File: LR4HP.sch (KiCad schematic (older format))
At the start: 15 parts

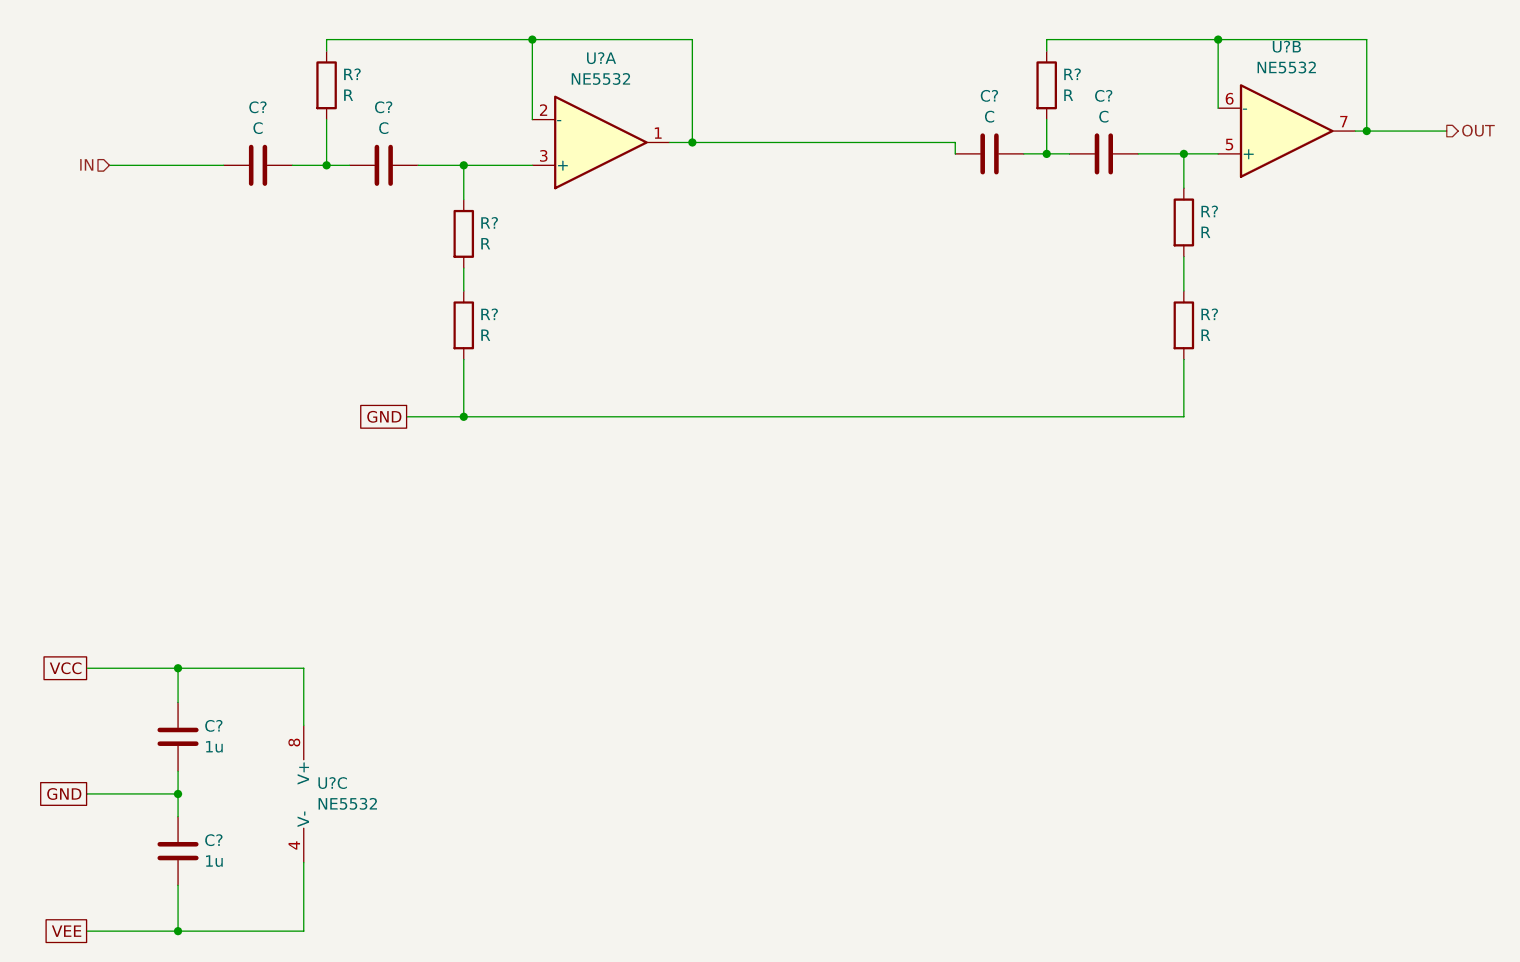
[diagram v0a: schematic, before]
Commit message: improved PSU, gain up front, reordered filter stages, shrunk rumble filter
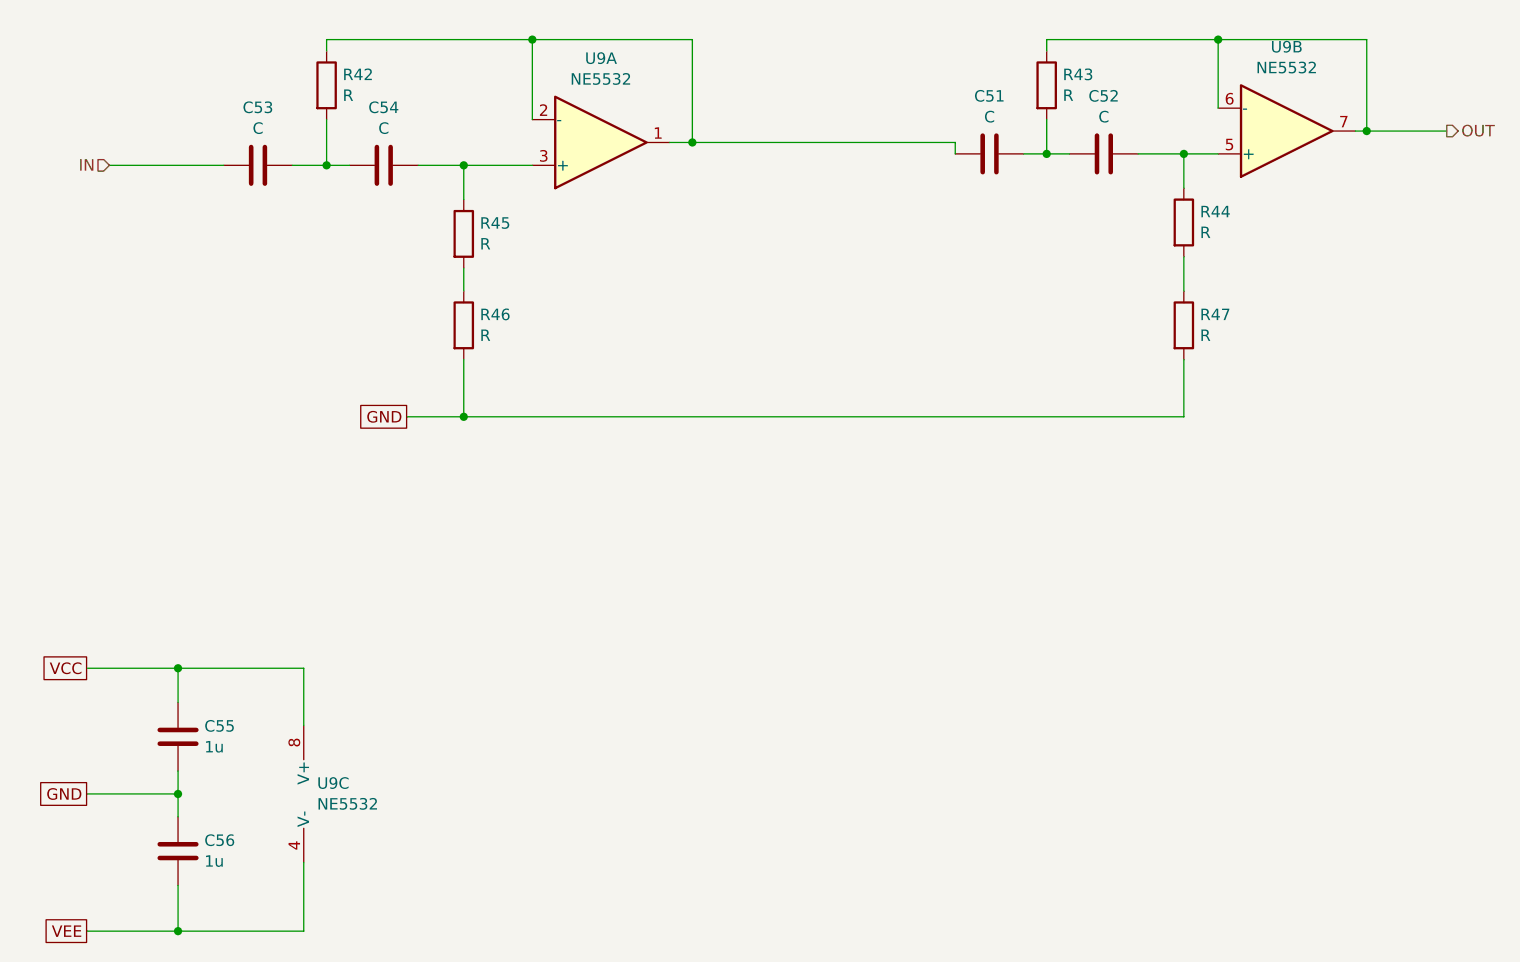
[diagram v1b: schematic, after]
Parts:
- gave numbers to parts that had none: 13

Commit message: added buffered volume pot, and fixed subsonic filter added signal taps for external transforms/filters to be added later
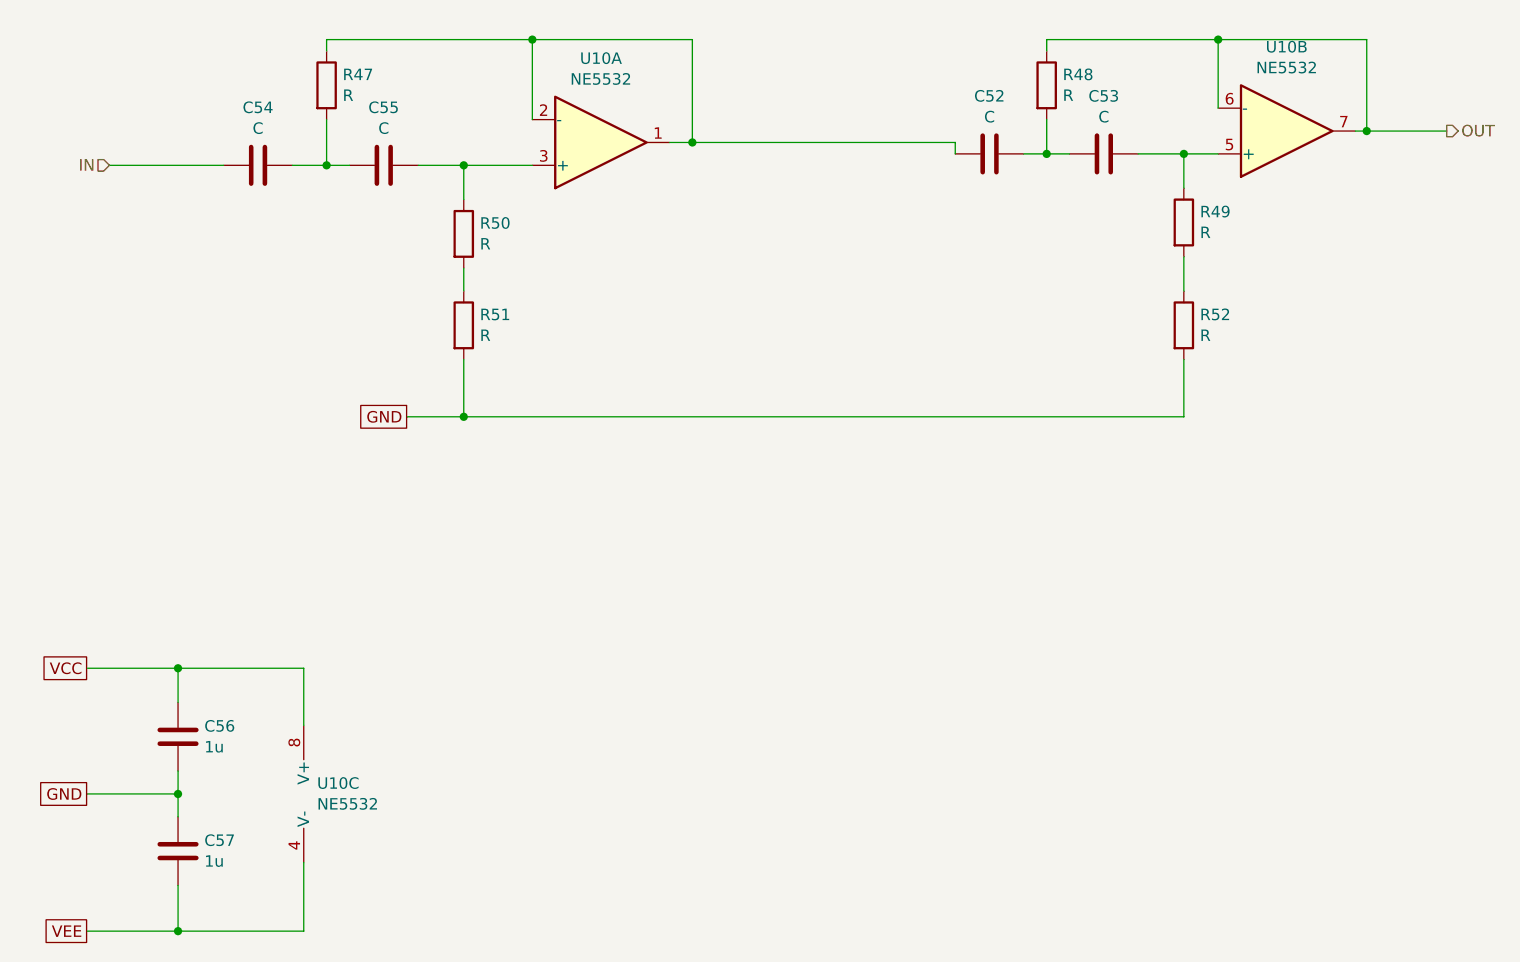
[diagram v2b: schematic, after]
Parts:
- renumbered C45 to C46, C46 to C47, C47 to C48, C48 to C49, C49 to C50, C50 to C51, R36 to R41, R37 to R42, R38 to R43, R39 to R44, R40 to R45, R41 to R46, U8 to U9

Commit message: inverted LF processing chain, now with BW2 subsonic filter
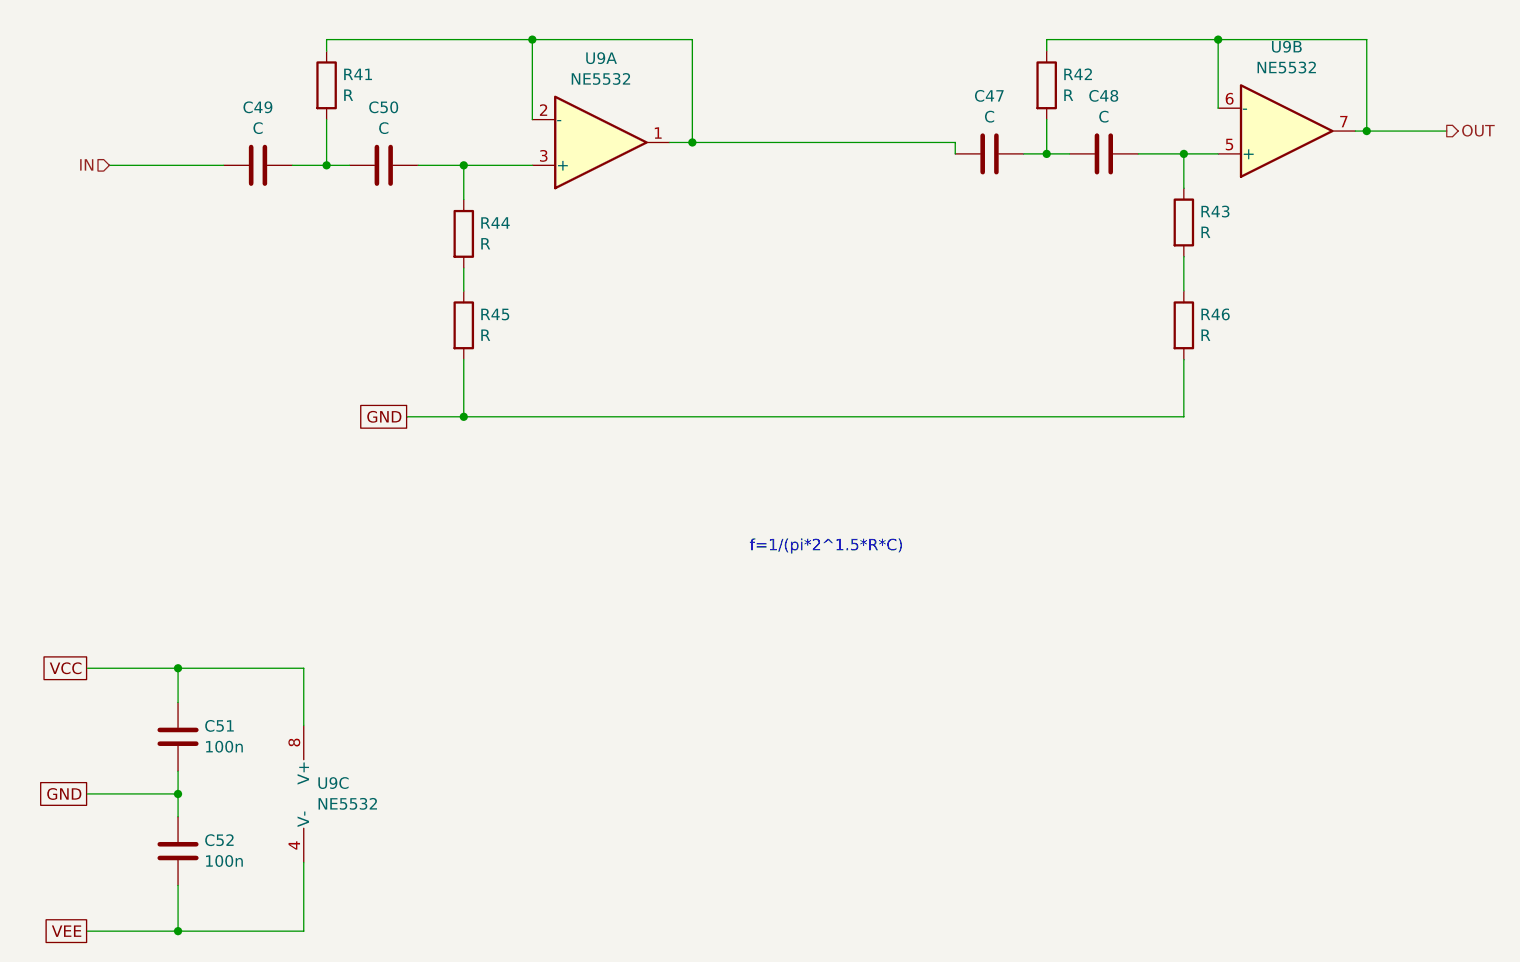
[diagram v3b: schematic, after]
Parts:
- C51: renamed from C50; value 1u -> 100n
- C52: renamed from C51; value 1u -> 100n
- renumbered C46 to C47, C47 to C48, C48 to C49, C49 to C50
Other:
- note added: "f=1/(pi*2^1.5*R*C)"
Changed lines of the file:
@@
 $Descr A4 11693 8268
 encoding utf-8
-Sheet 9 19
+Sheet 8 17
 Title "4th Order Linkwitz-Riley High-Pass"
 Date "2021-10-03"
@@
 AR Path="/61597701/61581F20" Ref="U10"  Part="3"
 AR Path="/615C4B54/61581F20" Ref="U?"  Part="3"
-F 0 "U10" H 3358 4996 50  0000 L CNN
+F 0 "U9" H 3358 4996 50  0000 L CNN
 F 1 "NE5532" H 3358 4905 50  0000 L CNN
 F 2 "Housings_DIP:DIP-8_W7.62mm_Socket" H 3400 4950 50  0001 C CNN
@@
 $EndComp
 $Comp
-L Device:C C51
+L Device:C C52
 U 1 1 615A630E
 P 2750 5200
-AR Path="/6157B871/615A630E" Ref="C51"  Part="1"
-AR Path="/615961F1/615A630E" Ref="C17"  Part="1"
-AR Path="/61596D2A/615A630E" Ref="C31"  Part="1"
-AR Path="/61597701/615A630E" Ref="C57"  Part="1"
+AR Path="/6157B871/615A630E" Ref="C52"  Part="1"
+AR Path="/615961F1/615A630E" Ref="C18"  Part="1"
+AR Path="/61596D2A/615A630E" Ref="C32"  Part="1"
+AR Path="/61597701/615A630E" Ref="C58"  Part="1"
 AR Path="/615C4B54/615A630E" Ref="C?"  Part="1"
-F 0 "C57" H 2865 5246 50  0000 L CNN
-F 1 "1u" H 2865 5155 50  0000 L CNN
+F 0 "C52" H 2865 5246 50  0000 L CNN
+F 1 "100n" H 2865 5155 50  0000 L CNN
 F 2 "Capacitors_SMD:C_0805" H 2788 5050 50  0001 C CNN
 F 3 "~" H 2750 5200 50  0001 C CNN
@@
 AR Path="/61597701/61593BE2" Ref="R51"  Part="1"
 AR Path="/615C4B54/61593BE2" Ref="R?"  Part="1"
-F 0 "R51" H 4070 2946 50  0000 L CNN
+F 0 "R45" H 4070 2946 50  0000 L CNN
 F 1 "R" H 4070 2855 50  0000 L CNN
 F 2 "Resistors_SMD:R_0805" V 3930 2900 50  0001 C CNN
@@
 AR Path="/61597701/615935AE" Ref="R50"  Part="1"
 AR Path="/615C4B54/615935AE" Ref="R?"  Part="1"
-F 0 "R50" H 4070 2546 50  0000 L CNN
+F 0 "R44" H 4070 2546 50  0000 L CNN
 F 1 "R" H 4070 2455 50  0000 L CNN
 F 2 "Resistors_SMD:R_0805" V 3930 2500 50  0001 C CNN
@@
 AR Path="/61597701/61592F52" Ref="R47"  Part="1"
 AR Path="/615C4B54/61592F52" Ref="R?"  Part="1"
-F 0 "R47" H 3470 1896 50  0000 L CNN
+F 0 "R41" H 3470 1896 50  0000 L CNN
 F 1 "R" H 3470 1805 50  0000 L CNN
 F 2 "Resistors_SMD:R_0805" V 3330 1850 50  0001 C CNN
@@
 $EndComp
 $Comp
-L Device:C C49
+L Device:C C50
 U 1 1 61590C79
 P 3650 2200
-AR Path="/6157B871/61590C79" Ref="C49"  Part="1"
-AR Path="/615961F1/61590C79" Ref="C15"  Part="1"
-AR Path="/61596D2A/61590C79" Ref="C29"  Part="1"
-AR Path="/61597701/61590C79" Ref="C55"  Part="1"
+AR Path="/6157B871/61590C79" Ref="C50"  Part="1"
+AR Path="/615961F1/61590C79" Ref="C16"  Part="1"
+AR Path="/61596D2A/61590C79" Ref="C30"  Part="1"
+AR Path="/61597701/61590C79" Ref="C56"  Part="1"
 AR Path="/615C4B54/61590C79" Ref="C?"  Part="1"
-F 0 "C55" V 3398 2200 50  0000 C CNN
+F 0 "C50" V 3398 2200 50  0000 C CNN
 F 1 "C" V 3489 2200 50  0000 C CNN
 F 2 "Capacitors_SMD:C_1210_HandSoldering" H 3688 2050 50  0001 C CNN
@@
 $EndComp
 $Comp
-L Device:C C48
+L Device:C C49
 U 1 1 6158BBA5
 P 3100 2200
-AR Path="/6157B871/6158BBA5" Ref="C48"  Part="1"
-AR Path="/615961F1/6158BBA5" Ref="C14"  Part="1"
-AR Path="/61596D2A/6158BBA5" Ref="C28"  Part="1"
-AR Path="/61597701/6158BBA5" Ref="C54"  Part="1"
+AR Path="/6157B871/6158BBA5" Ref="C49"  Part="1"
+AR Path="/615961F1/6158BBA5" Ref="C15"  Part="1"
+AR Path="/61596D2A/6158BBA5" Ref="C29"  Part="1"
+AR Path="/61597701/6158BBA5" Ref="C55"  Part="1"
 AR Path="/615C4B54/6158BBA5" Ref="C?"  Part="1"
-F 0 "C54" V 2848 2200 50  0000 C CNN
+F 0 "C49" V 2848 2200 50  0000 C CNN
 F 1 "C" V 2939 2200 50  0000 C CNN
 F 2 "Capacitors_SMD:C_1210_HandSoldering" H 3138 2050 50  0001 C CNN
@@
 AR Path="/61597701/61581F14" Ref="U10"  Part="1"
 AR Path="/615C4B54/61581F14" Ref="U?"  Part="1"
-F 0 "U10" H 4600 1733 50  0000 C CNN
+F 0 "U9" H 4600 1733 50  0000 C CNN
 F 1 "NE5532" H 4600 1824 50  0000 C CNN
 F 2 "Housings_DIP:DIP-8_W7.62mm_Socket" H 4600 2100 50  0001 C CNN
@@
 $EndComp
 $Comp
-L Device:C C47
+L Device:C C48
 U 1 1 615B29CF
 P 6800 2150
-AR Path="/6157B871/615B29CF" Ref="C47"  Part="1"
-AR Path="/615961F1/615B29CF" Ref="C13"  Part="1"
-AR Path="/61596D2A/615B29CF" Ref="C27"  Part="1"
-AR Path="/61597701/615B29CF" Ref="C53"  Part="1"
+AR Path="/6157B871/615B29CF" Ref="C48"  Part="1"
+AR Path="/615961F1/615B29CF" Ref="C14"  Part="1"
+AR Path="/61596D2A/615B29CF" Ref="C28"  Part="1"
+AR Path="/61597701/615B29CF" Ref="C54"  Part="1"
 AR Path="/615C4B54/615B29CF" Ref="C?"  Part="1"
-F 0 "C53" V 6548 2150 50  0000 C CNN
+F 0 "C48" V 6548 2150 50  0000 C CNN
 F 1 "C" V 6639 2150 50  0000 C CNN
 F 2 "Capacitors_SMD:C_1210_HandSoldering" H 6838 2000 50  0001 C CNN
@@
 $EndComp
 $Comp
-L Device:C C46
+L Device:C C47
 U 1 1 615B9BE0
 P 6300 2150
-AR Path="/6157B871/615B9BE0" Ref="C46"  Part="1"
-AR Path="/615961F1/615B9BE0" Ref="C12"  Part="1"
-AR Path="/61596D2A/615B9BE0" Ref="C26"  Part="1"
-AR Path="/61597701/615B9BE0" Ref="C52"  Part="1"
+AR Path="/6157B871/615B9BE0" Ref="C47"  Part="1"
+AR Path="/615961F1/615B9BE0" Ref="C13"  Part="1"
+AR Path="/61596D2A/615B9BE0" Ref="C27"  Part="1"
+AR Path="/61597701/615B9BE0" Ref="C53"  Part="1"
 AR Path="/615C4B54/615B9BE0" Ref="C?"  Part="1"
-F 0 "C52" V 6048 2150 50  0000 C CNN
+F 0 "C47" V 6048 2150 50  0000 C CNN
 F 1 "C" V 6139 2150 50  0000 C CNN
 F 2 "Capacitors_SMD:C_1210_HandSoldering" H 6338 2000 50  0001 C CNN
@@
 AR Path="/61597701/615C3593" Ref="R48"  Part="1"
 AR Path="/615C4B54/615C3593" Ref="R?"  Part="1"
-F 0 "R48" H 6620 1896 50  0000 L CNN
+F 0 "R42" H 6620 1896 50  0000 L CNN
 F 1 "R" H 6620 1805 50  0000 L CNN
 F 2 "Resistors_SMD:R_0805" V 6480 1850 50  0001 C CNN
@@
 AR Path="/61597701/615C391A" Ref="R49"  Part="1"
 AR Path="/615C4B54/615C391A" Ref="R?"  Part="1"
-F 0 "R49" H 7220 2496 50  0000 L CNN
+F 0 "R43" H 7220 2496 50  0000 L CNN
 F 1 "R" H 7220 2405 50  0000 L CNN
 F 2 "Resistors_SMD:R_0805" V 7080 2450 50  0001 C CNN
@@
 AR Path="/61597701/615C3D1F" Ref="R52"  Part="1"
 AR Path="/615C4B54/615C3D1F" Ref="R?"  Part="1"
-F 0 "R52" H 7220 2946 50  0000 L CNN
+F 0 "R46" H 7220 2946 50  0000 L CNN
 F 1 "R" H 7220 2855 50  0000 L CNN
 F 2 "Resistors_SMD:R_0805" V 7080 2900 50  0001 C CNN
@@
 	7150 3300 7150 3050
 $Comp
-L Device:C C50
+L Device:C C51
 U 1 1 615CA1F0
 P 2750 4700
-AR Path="/6157B871/615CA1F0" Ref="C50"  Part="1"
-AR Path="/615961F1/615CA1F0" Ref="C16"  Part="1"
-AR Path="/61596D2A/615CA1F0" Ref="C30"  Part="1"
-AR Path="/61597701/615CA1F0" Ref="C56"  Part="1"
+AR Path="/6157B871/615CA1F0" Ref="C51"  Part="1"
+AR Path="/615961F1/615CA1F0" Ref="C17"  Part="1"
+AR Path="/61596D2A/615CA1F0" Ref="C31"  Part="1"
+AR Path="/61597701/615CA1F0" Ref="C57"  Part="1"
 AR Path="/615C4B54/615CA1F0" Ref="C?"  Part="1"
-F 0 "C56" H 2865 4746 50  0000 L CNN
-F 1 "1u" H 2865 4655 50  0000 L CNN
+F 0 "C51" H 2865 4746 50  0000 L CNN
+F 1 "100n" H 2865 4655 50  0000 L CNN
 F 2 "Capacitors_SMD:C_0805" H 2788 4550 50  0001 C CNN
 F 3 "~" H 2750 4700 50  0001 C CNN
@@
 AR Path="/61597701/61581F1A" Ref="U10"  Part="2"
 AR Path="/615C4B54/61581F1A" Ref="U?"  Part="2"
-F 0 "U10" H 7600 1683 50  0000 C CNN
+F 0 "U9" H 7600 1683 50  0000 C CNN
 F 1 "NE5532" H 7600 1774 50  0000 C CNN
 F 2 "Housings_DIP:DIP-8_W7.62mm_Socket" H 7600 2050 50  0001 C CNN
@@
 Wire Wire Line
 	2450 2200 2950 2200
+Text Notes 5250 3900 0    50   ~ 0
+f=1/(pi*2^1.5*R*C)
 $EndSCHEMATC
